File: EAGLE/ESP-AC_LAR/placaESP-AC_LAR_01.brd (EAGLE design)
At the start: 42.5 x 44.5 mm, 13 parts, among them Q1 2N4401

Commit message: Placa refeita (rotas) 2
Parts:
- turned RESET to 180 degrees
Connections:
- net CTS: no longer RESET.1
- net N$6: no longer FLASH.3
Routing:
- net CTS: track 66.0 -> 57.6 mm
- net N$6: track 55.0 -> 47.6 mm
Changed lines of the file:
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@@
 <element name="MDL1" library="ESP8266-ESP12E" package="ESP8266-ESP12E" value="" x="16.51" y="31.75" rot="R90"/>
 <element name="Q1" library="transistor-npn" package="TO92" value="2N4401" x="23.37" y="8.78"/>
-<element name="RESET" library="switch-omron" package="B3F-10XX" value="" x="36.95" y="27.4">
-<attribute name="OC_NEWARK" value="36M3542" x="36.95" y="27.4" size="1.778" layer="27" display="off"/>
-<attribute name="MPN" value="B3F-1000" x="36.95" y="27.4" size="1.778" layer="27" display="off"/>
-<attribute name="MF" value="" x="36.95" y="27.4" size="1.778" layer="27" display="off"/>
-<attribute name="OC_FARNELL" value="176432" x="36.95" y="27.4" size="1.778" layer="27" display="off"/>
+<element name="RESET" library="switch-omron" package="B3F-10XX" value="" x="36.95" y="27.4" rot="R180">
+<attribute name="OC_NEWARK" value="36M3542" x="36.95" y="27.4" size="1.778" layer="27" rot="R180" display="off"/>
+<attribute name="MPN" value="B3F-1000" x="36.95" y="27.4" size="1.778" layer="27" rot="R180" display="off"/>
+<attribute name="MF" value="" x="36.95" y="27.4" size="1.778" layer="27" rot="R180" display="off"/>
+<attribute name="OC_FARNELL" value="176432" x="36.95" y="27.4" size="1.778" layer="27" rot="R180" display="off"/>
 </element>
 <element name="FLASH" library="switch-omron" package="B3F-10XX" value="" x="36.95" y="38.83" rot="R180">
@@
 <contactref element="MDL1" pad="1"/>
 <contactref element="RESET" pad="2"/>
-<contactref element="RESET" pad="1"/>
 <contactref element="FTDI" pad="5"/>
 <contactref element="R1" pad="2"/>
-<wire x1="34.29" y1="29.4894" x2="33.8328" y2="29.4894" width="0.254" layer="16"/>
-<wire x1="35.433" y1="28.3464" x2="34.29" y2="29.4894" width="0.254" layer="16"/>
-<wire x1="37.9476" y1="28.3464" x2="35.433" y2="28.3464" width="0.254" layer="16"/>
-<wire x1="39.0906" y1="29.4894" x2="37.9476" y2="28.3464" width="0.254" layer="16"/>
-<wire x1="40.005" y1="29.4894" x2="39.0906" y2="29.4894" width="0.254" layer="16"/>
-<wire x1="33.8328" y1="29.4894" x2="33.6988" y2="29.6606" width="0.254" layer="16"/>
-<wire x1="40.005" y1="29.4894" x2="40.2012" y2="29.6606" width="0.254" layer="16"/>
 <wire x1="10.0584" y1="23.5458" x2="10.5156" y2="24.003" width="0.254" layer="1"/>
 <wire x1="8.9154" y1="23.5458" x2="10.0584" y2="23.5458" width="0.254" layer="1"/>
@@
 <wire x1="17.3736" y1="2.9718" x2="17.47" y2="2.81" width="0.254" layer="16"/>
 <wire x1="3.2004" y1="18.5166" x2="3.25" y2="18.558" width="0.254" layer="16"/>
-<wire x1="33.147" y1="29.4894" x2="33.6042" y2="29.4894" width="0.254" layer="1"/>
-<wire x1="29.2608" y1="25.6032" x2="33.147" y2="29.4894" width="0.254" layer="1"/>
-<wire x1="25.146" y1="25.6032" x2="29.2608" y2="25.6032" width="0.254" layer="1"/>
-<wire x1="24.6888" y1="26.0604" x2="25.146" y2="25.6032" width="0.254" layer="1"/>
-<wire x1="11.2014" y1="26.0604" x2="24.6888" y2="26.0604" width="0.254" layer="1"/>
+<wire x1="32.2326" y1="24.9174" x2="33.6042" y2="24.9174" width="0.254" layer="1"/>
+<wire x1="31.5468" y1="24.2316" x2="32.2326" y2="24.9174" width="0.254" layer="1"/>
+<wire x1="26.7462" y1="24.2316" x2="31.5468" y2="24.2316" width="0.254" layer="1"/>
+<wire x1="24.9174" y1="26.0604" x2="26.7462" y2="24.2316" width="0.254" layer="1"/>
+<wire x1="11.2014" y1="26.0604" x2="24.9174" y2="26.0604" width="0.254" layer="1"/>
 <wire x1="10.7442" y1="25.6032" x2="11.2014" y2="26.0604" width="0.254" layer="1"/>
 <wire x1="10.7442" y1="24.2316" x2="10.7442" y2="25.6032" width="0.254" layer="1"/>
-<wire x1="33.6042" y1="29.4894" x2="33.6988" y2="29.6606" width="0.254" layer="1"/>
+<wire x1="33.6042" y1="24.9174" x2="33.6988" y2="25.1394" width="0.254" layer="1"/>
 <wire x1="10.7442" y1="24.2316" x2="10.67" y2="24.13" width="0.254" layer="1"/>
 </signal>
@@
 </signal>
 <signal name="N$6">
-<contactref element="FLASH" pad="3"/>
 <contactref element="FLASH" pad="4"/>
 <contactref element="MDL1" pad="12"/>
@@
 <wire x1="14.859" y1="18.5166" x2="14.75" y2="18.48" width="0.254" layer="16"/>
 <wire x1="33.6042" y1="40.9194" x2="33.6988" y2="41.0906" width="0.254" layer="16"/>
-<wire x1="38.862" y1="40.9194" x2="40.005" y2="40.9194" width="0.254" layer="1"/>
-<wire x1="37.9476" y1="40.005" x2="38.862" y2="40.9194" width="0.254" layer="1"/>
-<wire x1="35.6616" y1="40.005" x2="37.9476" y2="40.005" width="0.254" layer="1"/>
-<wire x1="34.7472" y1="40.9194" x2="35.6616" y2="40.005" width="0.254" layer="1"/>
-<wire x1="33.8328" y1="40.9194" x2="34.7472" y2="40.9194" width="0.254" layer="1"/>
-<wire x1="40.005" y1="40.9194" x2="40.2012" y2="41.0906" width="0.254" layer="1"/>
-<wire x1="33.8328" y1="40.9194" x2="33.6988" y2="41.0906" width="0.254" layer="1"/>
 </signal>
 </signals>

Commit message: Modificações - dia 03/02/17
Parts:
- added IC1: (no value), kaibader:AMS1117
- added X1: 22-23-2021, con-molex:22-23-2021
- moved Q1 8.54 mm to (31.7, 6.97), turned to 90 degrees
- moved FTDI 3.82 mm to (17.5, 3.21)
- moved R2 3.30 mm to (7.01, 16.8)
- moved R3 3.30 mm to (10.9, 16.8)
- moved R1 3.30 mm to (3.25, 16.8)
- moved R6 3.30 mm to (14.8, 16.7)
- moved IR 2.37 mm to (37.5, 10.0)
- moved R5 1.99 mm to (25.3, 16.8)
- moved R4 1.99 mm to (25.2, 20.6)
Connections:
- new net IN+: IC1.VIN, X1.2
- new net IN-: IC1.GND, X1.1
- net VCC: now also IC1.HEATSINK, IC1.VOUT
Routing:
- net IN-: track 0.00 -> 26.2 mm
- net IO4: track 27.1 -> 45.2 mm, vias 1 -> 0
- net IN+: track 0.00 -> 16.2 mm, vias 0 -> 1
- net VCC: track 48.1 -> 60.7 mm
- net TXO: track 48.8 -> 61.1 mm
- net N$3: track 9.94 -> 18.0 mm
- net RXI: track 54.9 -> 61.8 mm
- net N$4: track 12.7 -> 6.86 mm
- net CTS: track 57.6 -> 63.4 mm
- net N$6: track 47.6 -> 44.8 mm
- net N$5: track 26.6 -> 24.3 mm, vias 1 -> 0
- net N$2: track 9.05 -> 10.2 mm

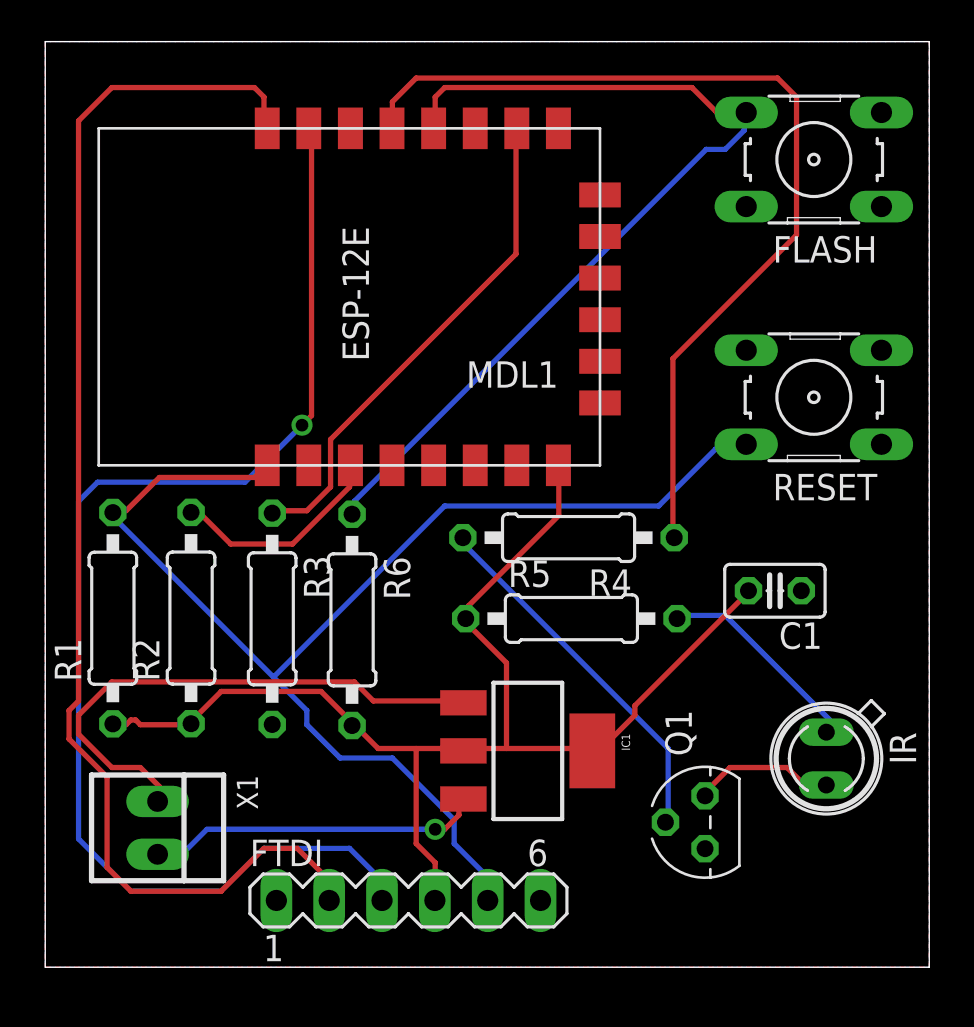
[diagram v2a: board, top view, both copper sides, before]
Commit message: Alterações dia 07/02 + placa porta + referências
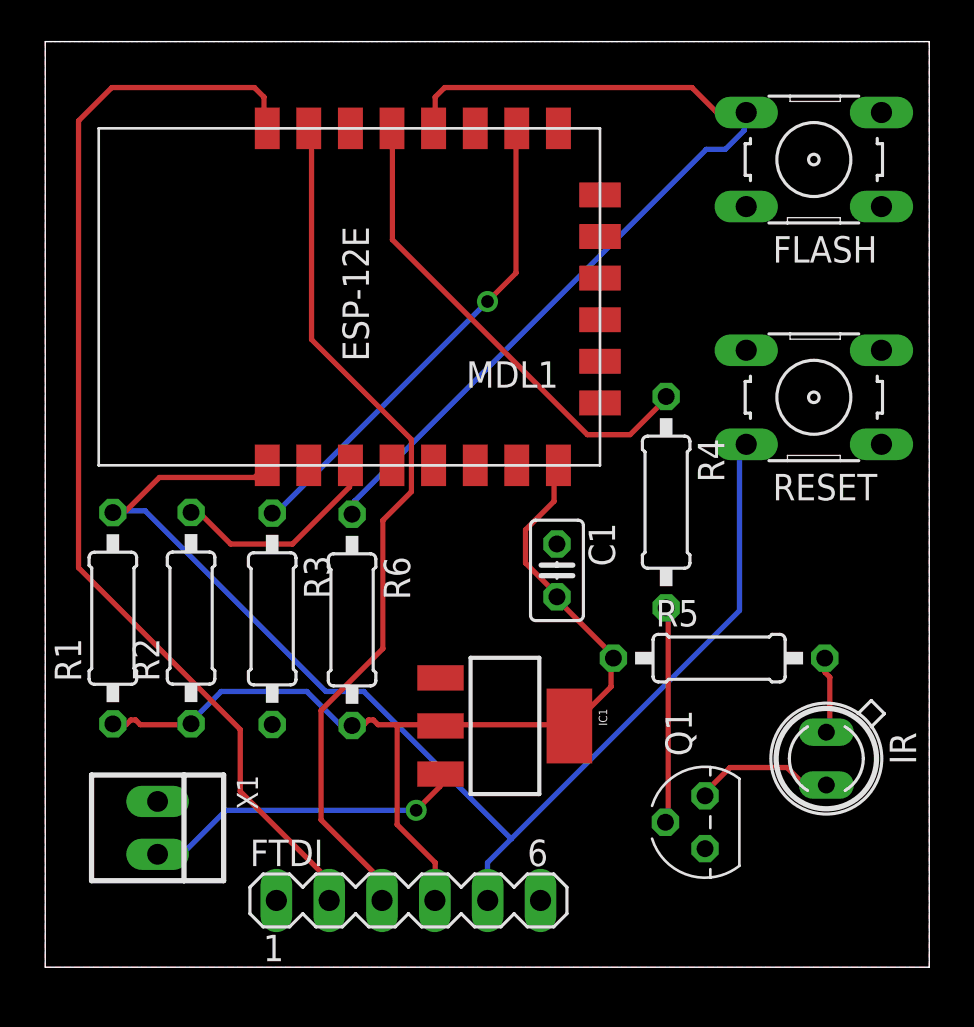
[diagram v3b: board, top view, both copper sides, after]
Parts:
- moved C1 10.5 mm to (24.6, 19.1), turned to 270 degrees
- moved R5 7.35 mm to (32.4, 14.9)
- moved R4 4.99 mm to (29.9, 22.4), turned to 270 degrees
- moved IC1 1.63 mm to (22.1, 11.6)
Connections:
- removed net IN-: IC1.GND, X1.1
- net GND: now also IC1.GND, X1.1
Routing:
- net IN-: track 26.2 -> 0.00 mm
- net IO4: track 45.2 -> 23.4 mm
- net TXO: track 61.1 -> 42.2 mm, vias 1 -> 0
- net VCC: track 60.7 -> 49.2 mm
- net RXI: track 61.8 -> 53.8 mm
- net N$3: track 18.0 -> 10.4 mm
- net N$2: track 10.2 -> 3.75 mm
- net CTS: track 63.4 -> 61.1 mm
- net N$5: track 24.3 -> 23.6 mm, vias 0 -> 1
- net IN+: track 16.2 -> 15.5 mm

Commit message: Add gerbers + atualização caixa
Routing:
- net RXI: track 53.8 -> 50.9 mm, vias 0 -> 1
- net VCC: track 49.2 -> 52.0 mm
- net TXO: track 42.2 -> 44.0 mm, vias 0 -> 2
- net CTS: track 61.1 -> 62.5 mm
- net N$4: track 6.86 -> 8.14 mm
- net IO4: track 23.4 -> 24.4 mm
- net N$1: track 10.5 -> 11.5 mm
- net N$3: track 10.4 -> 11.2 mm
- net N$6: track 44.8 -> 45.5 mm
- net IN+: track 15.5 -> 15.2 mm, vias 1 -> 0
